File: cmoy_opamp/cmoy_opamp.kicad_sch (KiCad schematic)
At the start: 51 parts, among them J1 AudioJack3, J2 AudioJack3, SW1 SPST, U1 MC33178, U2 LMH6642, U3 LMH6642, U4 LMH6642

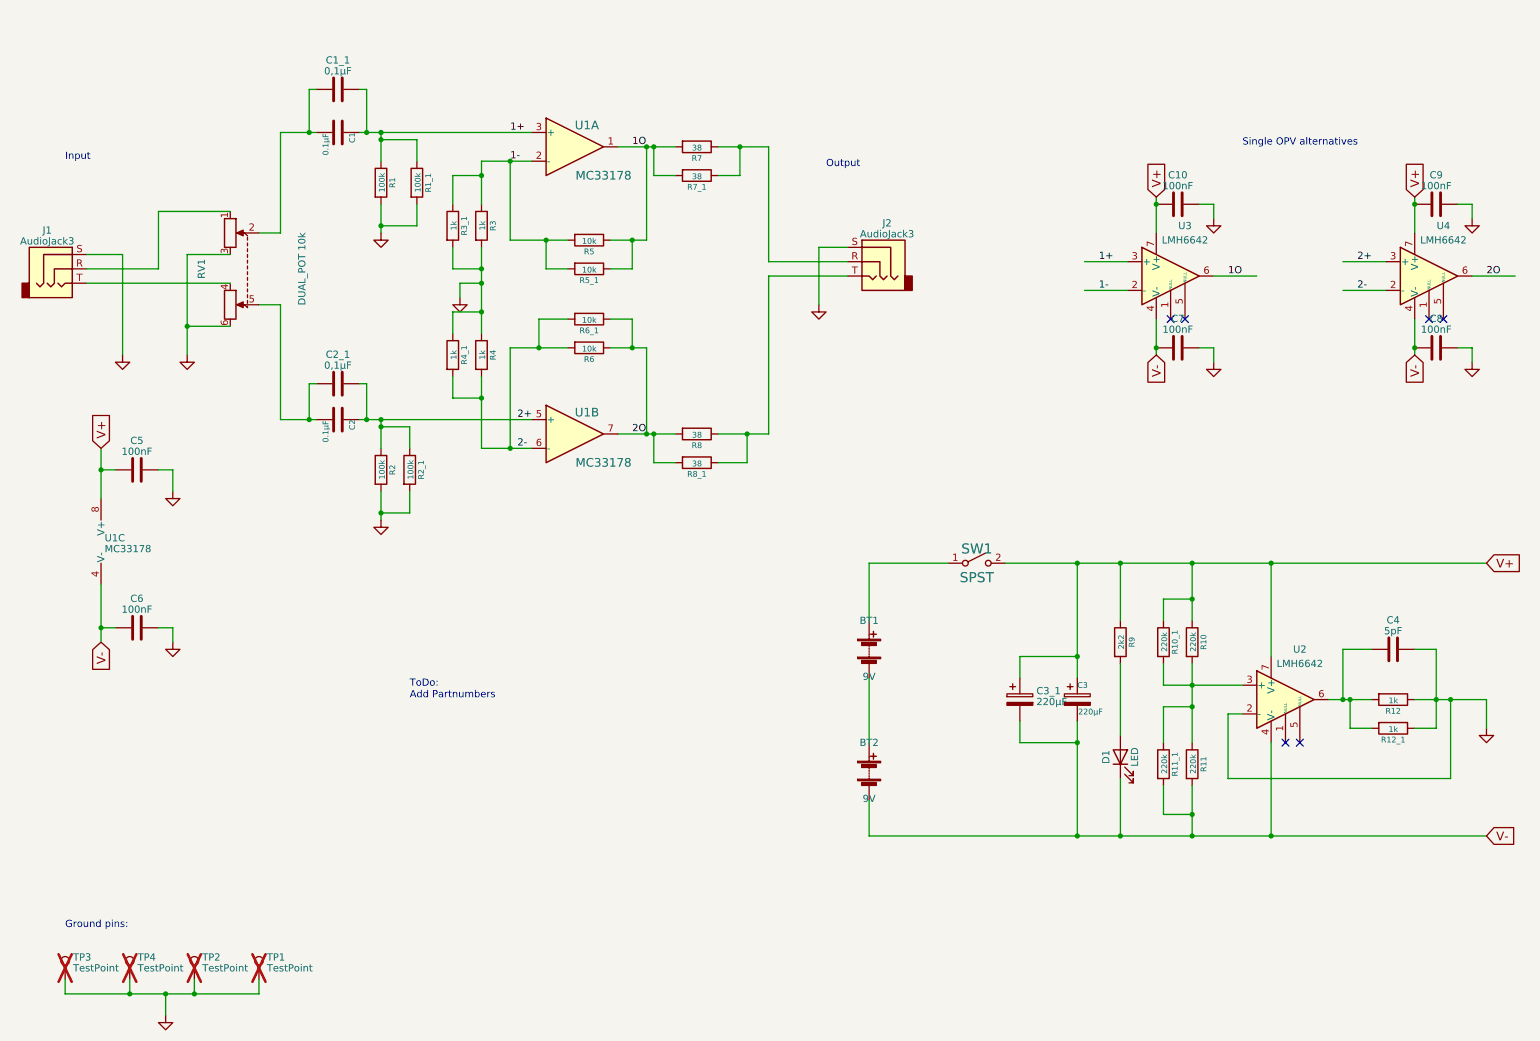
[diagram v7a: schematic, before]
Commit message: change drilling to fit zif socket
0,8mm increased to 1,1mm to fit the 0,9mm ZIF socket pins
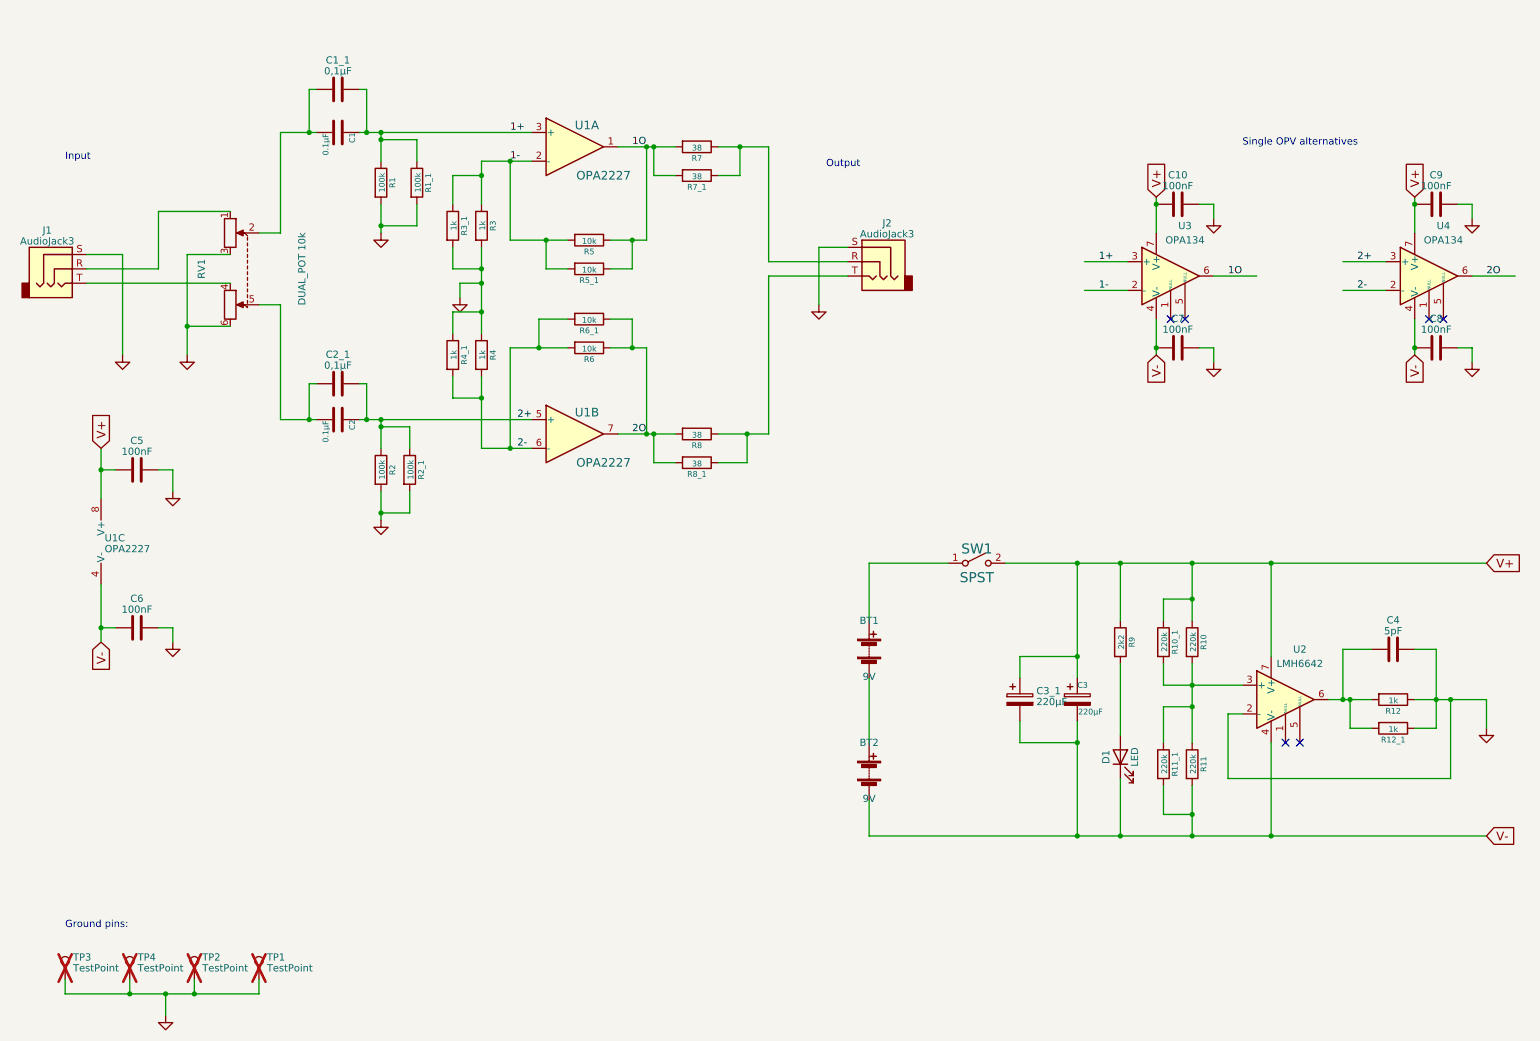
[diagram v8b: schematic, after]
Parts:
- U1: value MC33178 -> OPA2227
- U1: value MC33178 -> OPA2227; footprint (none) -> Package_DIP:DIP-8_W7.62mm_Socket
- U3, U4: value LMH6642 -> OPA134
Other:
- note removed: "ToDo: Add Partnumbers"
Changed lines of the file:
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@@
     (stroke (width 0) (type default))
-  )
-  (text "ToDo:\nAdd Partnumbers" (at 82.55 134.62 0)
-    (effects (font (size 1.27 1.27)) (justify left bottom))
   )
   (text "Input" (at 21.59 39.37 0)
@@
       (effects (font (size 1.524 1.524)) (justify left))
     )
-    (property "Value" "MC33178" (at 116.84 41.91 0)
+    (property "Value" "OPA2227" (at 116.84 41.91 0)
       (effects (font (size 1.524 1.524)))
     )
@@
       (effects (font (size 1.27 1.27)) hide)
     )
-    (property "Datasheet" "https://www.onsemi.com/pub/Collateral/MC33178-D.PDF" (at 111.76 36.83 0)
+    (property "Datasheet" "https://www.ti.com/lit/ds/symlink/opa2227.pdf" (at 111.76 36.83 0)
       (effects (font (size 1.27 1.27)) hide)
     )
@@
       (effects (font (size 1.524 1.524)) (justify left))
     )
-    (property "Value" "MC33178" (at 116.84 92.71 0)
+    (property "Value" "OPA2227" (at 116.84 92.71 0)
       (effects (font (size 1.524 1.524)))
     )
@@
       (effects (font (size 1.27 1.27)) hide)
     )
-    (property "Datasheet" "https://www.onsemi.com/pub/Collateral/MC33178-D.PDF" (at 111.76 87.63 0)
+    (property "Datasheet" "https://www.ti.com/lit/ds/symlink/opa2227.pdf" (at 111.76 87.63 0)
       (effects (font (size 1.27 1.27)) hide)
     )
@@
       (effects (font (size 1.27 1.27)) (justify left))
     )
-    (property "Value" "MC33178" (at 28.575 107.9573 0)
+    (property "Value" "OPA2227" (at 28.575 107.9573 0)
       (effects (font (size 1.27 1.27)) (justify left))
     )
-    (property "Footprint" "" (at 30.48 106.68 0)
-      (effects (font (size 1.27 1.27)) hide)
-    )
-    (property "Datasheet" "https://www.onsemi.com/pub/Collateral/MC33178-D.PDF" (at 30.48 106.68 0)
+    (property "Footprint" "Package_DIP:DIP-8_W7.62mm_Socket" (at 30.48 106.68 0)
+      (effects (font (size 1.27 1.27)) hide)
+    )
+    (property "Datasheet" "https://www.ti.com/lit/ds/symlink/opa2227.pdf" (at 30.48 106.68 0)
       (effects (font (size 1.27 1.27)) hide)
     )
@@
       (effects (font (size 1.27 1.27)))
     )
-    (property "Value" "LMH6642" (at 219.71 53.34 0)
+    (property "Value" "OPA134" (at 219.71 53.34 0)
       (effects (font (size 1.27 1.27)))
     )
@@
       (effects (font (size 1.27 1.27)) hide)
     )
-    (property "Datasheet" "https://www.ti.com/lit/ds/symlink/lmh6643.pdf" (at 220.98 55.88 0)
+    (property "Datasheet" "https://www.ti.com/lit/ds/symlink/opa134.pdf" (at 220.98 55.88 0)
       (effects (font (size 1.27 1.27)) hide)
     )
@@
       (effects (font (size 1.27 1.27)))
     )
-    (property "Value" "LMH6642" (at 265.43 53.34 0)
+    (property "Value" "OPA134" (at 265.43 53.34 0)
       (effects (font (size 1.27 1.27)))
     )
@@
       (effects (font (size 1.27 1.27)) hide)
     )
-    (property "Datasheet" "https://www.ti.com/lit/ds/symlink/lmh6643.pdf" (at 266.7 55.88 0)
-      (effects (font (size 1.27 1.27)) hide)
-    )
+    (property "Datasheet" "https://www.ti.com/lit/ds/symlink/opa134.pdf" (at 266.7 55.88 0)
+      (effects (font (size 1.27 1.27)) hide)
+    )
